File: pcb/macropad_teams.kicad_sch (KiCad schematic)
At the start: 32 parts, among them J1 Conn_01x04, SW1 SW_Push, SW10 SW_Push, SW11 SW_Push, SW12 SW_Push, SW13 SW_Push, SW14 SW_Push, SW2 SW_Push, SW3 SW_Push, SW4 SW_Push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

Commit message: On branch main  Changes to be committed: 	deleted:    pcb/macropad_teams-backups/macropad_teams-2025-09-16_111703.zip 	deleted:    pcb/macropad_teams-backups/macropad_teams-2025-09-16_113002.zip 	deleted:    pcb/macropad_teams-backups/macropad_teams-2025-10-22_192544.zip 	deleted:    pcb/macropad_teams-backups/macropad_teams-2025-10-22_211755.zip 	deleted:    pcb/macropad_teams-backups/macropad_teams-2025-11-05_183140.zip 	modified:   pcb/macropad_teams.kicad_pcb 	modified:   pcb/macropad_teams.kicad_prl 	modified:   pcb/macropad_teams.kicad_sch 	new file:   pcb/macropad_teams_messier.kicad_pcb 	new file:   pcb/macropad_teams_messier.kicad_pro
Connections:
- net JS_X: now reaches U1.11 (GP10)
- net JS_X: now also JS1.1 (X)
- net JS_Y: now reaches U1.12 (GP11)
- net JS_Y: now also JS1.3 (Y)
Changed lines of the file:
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@@
+	(wire
+		(pts
+			(xy 181.61 71.12) (xy 182.88 71.12)
+		)
+		(stroke
+			(width 0)
+			(type default)
+		)
+	)
 	(wire
 		(pts
@@
 		(pts
 			(xy 163.83 57.15) (xy 163.83 77.47)
+		)
+		(stroke
+			(width 0)
+			(type default)
+		)
+	)
+	(wire
+		(pts
+			(xy 181.61 68.58) (xy 182.88 68.58)
 		)
 		(stroke
@@
 		)
 	)
+	(label "JS_X"
+		(at 97.79 92.71 0)
+		(effects
+			(font
+				(size 1.27 1.27)
+			)
+			(justify left bottom)
+		)
+	)
+	(label "JS_Y"
+		(at 97.79 95.25 0)
+		(effects
+			(font
+				(size 1.27 1.27)
+			)
+			(justify left bottom)
+		)
+	)
 	(label "col2"
 		(at 62.23 97.79 0)
@@
 		)
 	)
+	(label "JS_X"
+		(at 181.61 68.58 0)
+		(effects
+			(font
+				(size 1.27 1.27)
+			)
+			(justify left bottom)
+		)
+	)
 	(label "row2"
 		(at 257.81 118.11 0)
 		(effects
 			(font
+				(size 1.27 1.27)
+			)
+			(justify left bottom)
+		)
+	)
+	(label "JS_Y"
+		(at 181.61 71.12 0)
+		(effects
+			(font

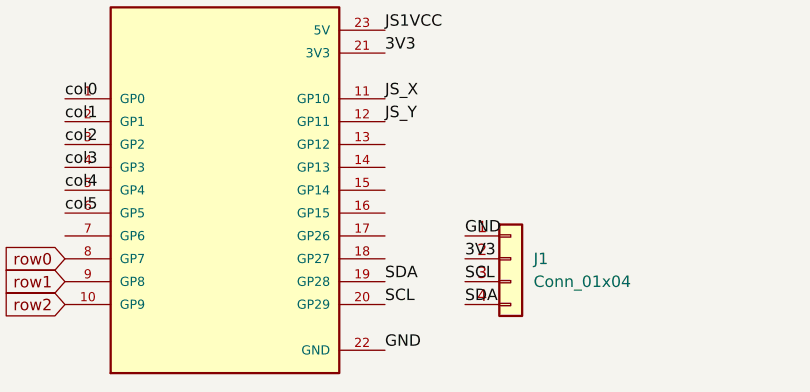
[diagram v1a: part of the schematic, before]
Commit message: On branch main Changes to be committed: deleted:    pcb/macropad_teams-backups/macropad_teams-2025-10-26_201154.zip deleted:    pcb/macropad_teams-backups/macropad_teams-2025-10-26_203901.zip deleted:    pcb/macropad_teams-backups/macropad_teams-2025-10-26_204439.zip modified:   pcb/macropad_teams.kicad_pcb modified:   pcb/macropad_teams.kicad_prl modified:   pcb/macropad_teams.kicad_sch
Much neater PCB routing this time around
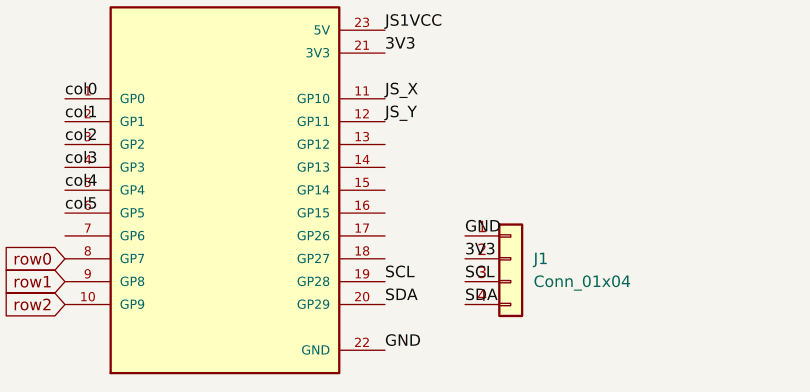
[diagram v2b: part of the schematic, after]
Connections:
- net SCL: now also U1.19 (GP28); no longer U1.20 (GP29)
- net SDA: now also U1.20 (GP29); no longer U1.19 (GP28)
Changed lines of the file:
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@@
 		)
 	)
-	(label "SCL"
+	(label "SDA"
 		(at 97.79 115.57 0)
 		(effects
@@
 		)
 	)
-	(label "SDA"
+	(label "SCL"
 		(at 97.79 113.03 0)
 		(effects
